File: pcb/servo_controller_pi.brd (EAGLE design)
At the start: 111 parts, among them IC1 PIC18F452, IC2 DS1339, IC3 MAX4173FESA+, IC4 LM2936MP-3.3, IC6 LM386M-1, IC7 GY-27, IC8 MCP23017SO, Q1 10Mhz

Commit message: BleuettePi new modification
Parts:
- removed IC8: MCP23017SO, adafruit:SO28W
- removed SV3: (no value), con-lstb:MA05-2
- added IC5: MCP23017SS, adafruit:SSOP28
- added X1: (no value), con-wago-500:W237-4
- SV1: device con-lstb:MA04-1 -> con-lstb:MA05-2
- SV2: device con-lstb:MA08-2 -> con-lstb:MA05-2
- moved SV1 78.2 mm to (75.6, 51.4), turned to 180 degrees
- moved TP1 20.3 mm to (1.75, 15.6)
- moved S11 10.5 mm to (66.4, 4.45)
- moved S10 10.2 mm to (62.9, 4.45)
- moved SV2 10.2 mm to (61.6, 51.4)
- moved S9 8.57 mm to (59.4, 4.45)
- moved S8 8.26 mm to (55.9, 4.45)
- moved SX 8.09 mm to (22.5, 10.8), turned to 0 degrees
- moved C3 7.85 mm to (11.4, 30.5), flipped to the bottom
- moved S7 6.03 mm to (52.4, 4.45)
- moved S6 5.71 mm to (48.9, 4.45)
- moved T_6V 5.40 mm to (46.4, 7.30)
- moved C9 5.08 mm to (43.2, 4.76)
- moved R1 4.94 mm to (11.4, 22.2), turned to 180 degrees
- moved S5 4.13 mm to (37.5, 4.45)
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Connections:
- removed net OUT: U$3.12
- new net OPTION4: U$3.21
- net +5V: now also IC5.18, IC5.9, SV1.10, SV2.10, X1.2; no longer IC8.18, IC8.9, SV1.2, SV3.10
- net +7V: now also X1.3; no longer SV1.3
- net GPA0: now also IC5.21, SV1.1; no longer IC8.21, SV2.2
- net GPA1: now also IC5.22, SV1.2; no longer IC8.22, SV2.4
- net GPA2: now also IC5.23, SV1.3; no longer IC8.23, SV2.6
- net GPA3: now also IC5.24, SV1.4; no longer IC8.24, SV2.8
- net GPA4: now also IC5.25, SV1.5; no longer IC8.25, SV2.10
- net GPA5: now also IC5.26, SV1.6; no longer IC8.26, SV2.12
- net GPA6: now also IC5.27, SV1.7; no longer IC8.27, SV2.14
- net GPA7: now also IC5.28, SV1.8; no longer IC8.28, SV2.16
- net GPB0: now also IC5.1, SV2.1; no longer IC8.1, SV3.2
- net GPB1: now also IC5.2, SV2.2; no longer IC8.2, SV3.1
- net GPB2: now also IC5.3, SV2.3; no longer IC8.3, SV3.4
- net GPB3: now also IC5.4, SV2.4; no longer IC8.4, SV3.3
- net GPB4: now also IC5.5, SV2.5; no longer IC8.5, SV3.6
- net GPB5: now also IC5.6, SV2.6; no longer IC8.6, SV3.5
- net GPB6: now also IC5.7, SV2.7; no longer IC8.7, SV3.8
- net GPB7: now also DRDY.1, IC5.8, SV2.8; no longer IC8.8, SV3.7
- net INTA: now also IC5.20; no longer IC8.20
- net INTB: now also IC5.19; no longer IC8.19
- net INTD: now also U$3.12; no longer DRDY.1
- net OPTION2: now also U$3.13; no longer U$3.16
- net OPTION3: now also U$3.15; no longer U$3.13
- net SCL: now also IC5.12; no longer IC8.12
- net SDA: now also IC5.13; no longer IC8.13
- net TRIGGER: now also U$3.16; no longer U$3.15
- net VDD: now also X1.4; no longer SV1.4
- net VSS: now also IC5.10, IC5.15, IC5.16, IC5.17, SV1.9, X1.1; no longer IC8.10, IC8.15, IC8.16, IC8.17, SV1.1, SV2.1, SV2.11, SV2.13, SV2.15, SV2.3, SV2.5, SV2.7, SV3.9
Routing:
- net +5V: track 306.3 -> 262.4 mm, vias 7 -> 6
- net VEE: track 172.1 -> 137.4 mm
- net INTB: track 57.0 -> 22.8 mm, vias 2 -> 0
- net INTA: track 51.6 -> 20.6 mm, vias 2 -> 0
- net OUT: track 25.7 -> 0.00 mm
- net +7V: track 40.8 -> 17.0 mm
- net GPB7: track 26.8 -> 10.8 mm
- net GPB6: track 27.4 -> 13.2 mm
- net +3V3: track 103.1 -> 91.2 mm
- net N$19: track 21.7 -> 10.8 mm
- net GPB4: track 21.5 -> 10.8 mm
- net SS11: track 35.6 -> 25.1 mm
- net SS10: track 31.5 -> 21.3 mm
- net VDD: track 8.65 -> 0.00 mm
- net SS9: track 25.7 -> 17.2 mm
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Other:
- board text added: "Isoler la partie ADC et SON"
- board text removed: "Isoler la partie ADC"

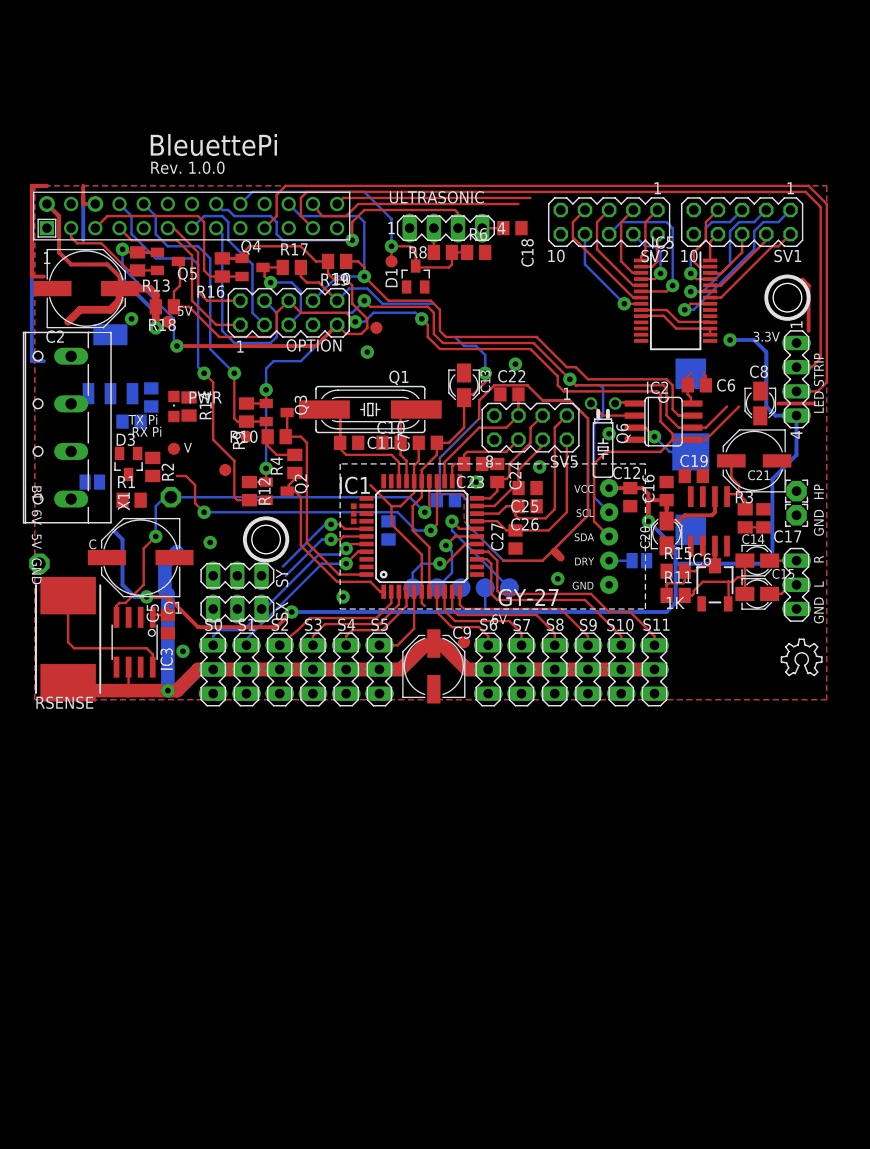
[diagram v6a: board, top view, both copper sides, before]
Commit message: Routage BleuettePi
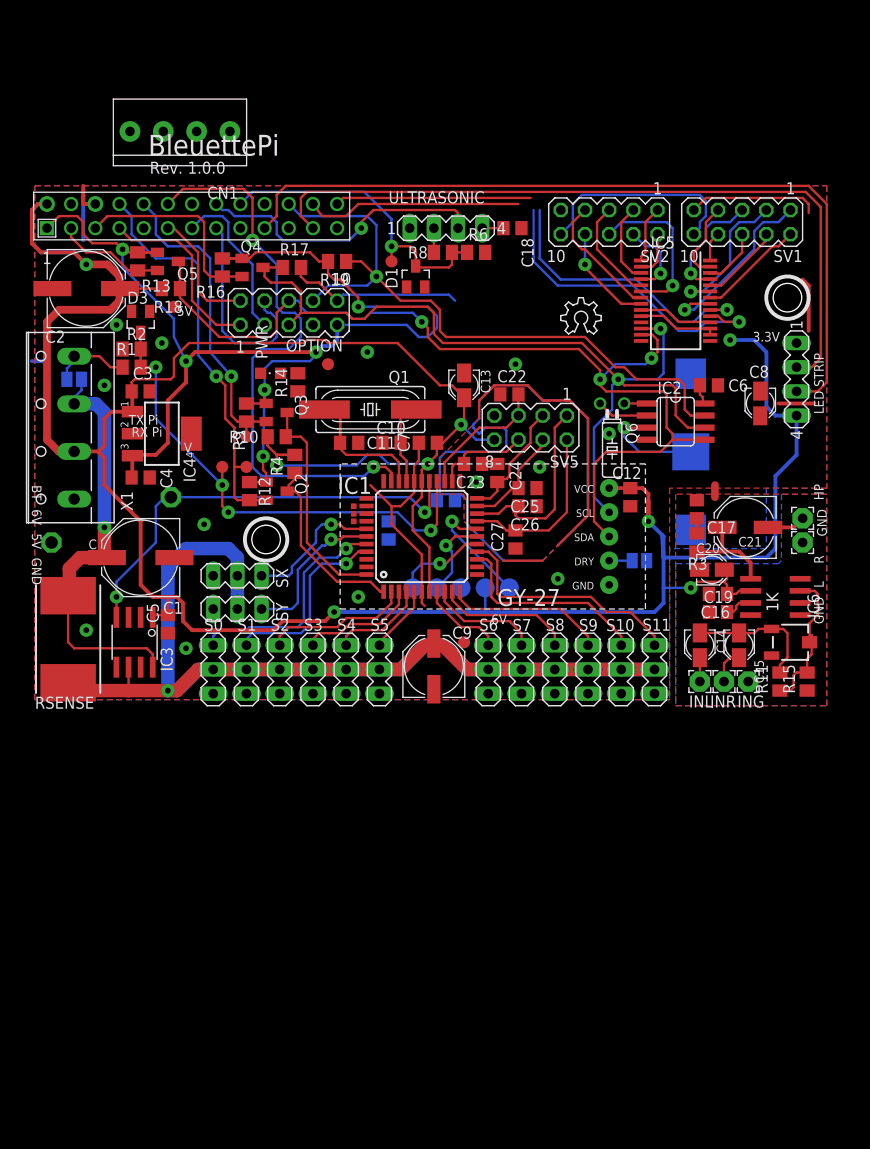
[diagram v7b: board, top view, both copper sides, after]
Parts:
- removed SV4: (no value), con-lstb:MA03-1
- added CN1: 1X4-3.5MM, adafruit:1X04-3.5MM
- added ING, INL, INR: (no value), wirepad:2,15/1,0
- moved U$5 42.7 mm to (56.5, 39.7)
- moved R15 18.0 mm to (82.4, 3.17), turned to 90 degrees
- moved D3 15.0 mm to (12.4, 41.0)
- moved C19 14.5 mm to (73.0, 10.5)
- moved R11 14.2 mm to (79.5, 3.17), turned to 90 degrees
- moved R1 14.0 mm to (11.4, 36.2)
- moved R2 12.6 mm to (11.4, 38.1), turned to 0 degrees
- moved C16 12.1 mm to (73.0, 12.4), turned to 180 degrees
- moved R14 11.7 mm to (28.9, 34.6), turned to 90 degrees
- moved J_SERV 11.0 mm to (5.40, 34.9)
- moved PWR 10.7 mm to (26.0, 35.6), turned to 90 degrees
- moved C14 10.7 mm to (71.1, 6.99), turned to 270 degrees
- moved IC6 10.6 mm to (79.1, 12.1), turned to 90 degrees
- moved 1K 9.97 mm to (80.6, 7.30), turned to 0 degrees
- moved IC4 9.08 mm to (14.6, 29.2), flipped to the top, turned to 270 degrees
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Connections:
- net N$40: now also INR.1; no longer SV4.2
- net N$7: now also 1K.1; no longer 1K.3
- net N$8: now also INL.1; no longer SV4.3
- net VSS: now also 1K.3, ING.1; no longer 1K.1, SV4.1
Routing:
- net +5V: track 262.4 -> 372.4 mm, vias 6 -> 8
- net INTD: track 0.00 -> 61.4 mm, vias 0 -> 2
- net +3V3: track 91.2 -> 133.5 mm, vias 4 -> 6
- net INTB: track 22.8 -> 56.5 mm, vias 0 -> 1
- net INTA: track 20.6 -> 50.4 mm, vias 0 -> 1
- net +7V: track 17.0 -> 44.8 mm, vias 0 -> 1
- net VSS: track 87.0 -> 67.0 mm, vias 8 -> 11
- net AN6: track 35.6 -> 53.0 mm, vias 2 -> 4
- net VEE: track 137.4 -> 149.0 mm
- net VDD: track 0.00 -> 8.29 mm
- net N$41: track 9.74 -> 16.7 mm
- net SCL: track 84.2 -> 90.5 mm, vias 3 -> 2
- net N$24: track 10.2 -> 16.2 mm
- net SDA: track 97.7 -> 102.1 mm, vias 2 -> 3
- net AGND: track 93.6 -> 97.8 mm
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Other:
- board text removed: "Isoler la partie ADC et SON"

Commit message: BleuettePi...
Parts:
- removed C3: 100nf, rcl:C0805
- removed C4: 10uf, rcl:C0805
- removed D1: 3V3, diode:SOT23
- removed IC4: LM2936MP-3.3, national-semiconductor:SOT223
- removed LED-STRIP, ULTRASONIC: (no value), con-lstb:MA04-1
- removed OPTION: (no value), con-lstb:MA05-2
- removed Q2, Q3, Q4, Q5: (no value), adafruit:SOT23
- removed R12, R4: 1k, rcl:M0805
- removed R13, R16, R17, R18: 10k, rcl:M0805
- removed R6: 3k3, rcl:M0805
- removed R8: 2k2, rcl:M0805
- removed T_ECHO, T_TX_PI: TPB1,27, testpad:B1,27
- removed U$7: (no value), adafruit:CR1220-SMD
- added C30, C31: 100nf, rcl:C0805
- added JP1: (no value), jumper:JP1
- added SJ1, SJ2: (no value), jumper:SJ_2
- added SV3: (no value), con-lstb:MA07-1
- added SV4: (no value), con-lstb:MA05-2
- added SV6: (no value), con-lstb:MA04-1
- added SV7: (no value), con-lstb:MA20-1
- added U$1: (no value), adafruit:CR1220-THM
- added U1, U2: (no value), adafruit:TSSOP20
- C18: value (none) -> 100nf
- C8: value (none) -> 100nf; device rcl:PANASONIC_A -> rcl:C0805
- R10: value 2k2 -> CALCUL_ME
- R9: value 3k3 -> CALCUL_ME
- moved C8 37.0 mm to (41.6, 41.3), turned to 180 degrees
- moved D3 21.3 mm to (25.4, 24.1), turned to 90 degrees
- moved R2 18.8 mm to (21.6, 22.2)
- moved R1 15.8 mm to (21.6, 24.1)
- moved T_5V 15.0 mm to (28.6, 34.6)
- moved R19 12.6 mm to (41.6, 38.1), turned to 0 degrees
- moved T_3.3V 12.2 mm to (44.1, 38.1)
- moved C18 11.3 mm to (40.6, 47.6), turned to 90 degrees
- moved C6 7.94 mm to (64.1, 34.0), turned to 0 degrees
- moved PWR 7.47 mm to (18.7, 37.1)
- moved R14 7.13 mm to (22.2, 37.1), turned to 180 degrees
- moved DRDY 5.02 mm to (60.0, 14.3), turned to 180 degrees
- moved Q6 4.48 mm to (63.7, 28.3), turned to 0 degrees
- moved R9 3.18 mm to (25.4, 28.9), turned to 0 degrees
- moved R10 2.29 mm to (25.4, 30.8)
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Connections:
- removed net DI: LED-STRIP.3, U$3.19
- removed net ECHO: D1.3, R6.2, R8.1, T_ECHO.TP, U$3.18
- removed net N$15: R8.2, ULTRASONIC.2
- removed net SI: LED-STRIP.2, U$3.23
- removed net TRIGGER: U$3.16, ULTRASONIC.3
- new net CE0: SV3.4, U2.16
- new net CE1: SV3.5, U2.15
- new net J_PI_CE1: SJ1.3, U2.6
- new net J_PI_INTA: SJ1.1, U2.7
- new net MISO: SV3.2, U2.18
- new net MOSI: SV3.1, U2.20
- new net PI_CE0: U$3.24, U2.5
- new net PI_CE1: SJ1.2, U$3.26
- new net PI_INTB: U$3.15, U2.8
- new net PI_INTD: U$3.12, U2.9
- new net PI_MISO: U$3.21, U2.3
- new net PI_MOSI: U$3.19, U2.1
- new net PI_OPTION0: U$3.7, U1.7
- new net PI_OPTION1: U$3.11, U1.6
- new net PI_OPTION2: U$3.13, U1.3
- new net PI_OPTION3: U$3.16, U1.4
- new net PI_OPTION4: U$3.18, U1.5
- new net PI_SCLK: U$3.23, U2.4
- new net SCLK: SV3.3, U2.17
- net +3V3: now also C30.1, C8.1, U1.10, U1.2, U2.10, U2.2; no longer C4.1, IC4.3, OPTION.9, Q2.1, Q3.1, Q4.1, Q5.1, R12.2, R13.2, R16.2, R9.2
- net +5V: now also C31.1, SV3.7, SV4.10, SV6.1, U1.19, U2.19; no longer C3.1, C8.+, IC4.1, LED-STRIP.4, OPTION.10, R10.2, R17.2, R18.2, R4.2, ULTRASONIC.4
- net +7V: now also JP1.1
- net INTA: now also U2.14; no longer U$3.26
- net INTB: now also U2.13; no longer U$3.24
- net INTC: now also SV4.6; no longer OPTION.8
- net INTD: now also U2.12; no longer U$3.12
- net N$16: now also R9.2; no longer Q3.3, R10.1
- net N$58: now also U$1.-; no longer U$7.-
- net OPTION0: now also SV4.1, U1.14; no longer OPTION.1, U$3.7
- net OPTION1: now also SV4.2, U1.15; no longer OPTION.2, U$3.11
- net OPTION2: now also SV4.3, U1.18; no longer OPTION.3, U$3.13
- net OPTION3: now also SV4.4, SV6.2, U1.17; no longer OPTION.4, U$3.15
- net OPTION4: now also SV4.5, SV6.3, U1.16; no longer U$3.21
- net PI_SCL: now also U1.8; no longer Q4.2, R16.1
- net PI_SDA: now also U1.9; no longer Q5.2, R13.1
- net RX_PI: now also R10.2; no longer Q3.2
- net RX_PIC: now also U1.20; no longer Q2.3, R4.1
- net SCL: now also SV4.7, U1.13; no longer OPTION.5, Q4.3, R17.1
- net SDA: now also SV4.8, U1.12; no longer OPTION.6, Q5.3, R18.1
- net TX_PI: now also U1.1; no longer Q2.2, R12.1, T_TX_PI.TP
- net VDD: now also JP1.2
- net VSS: now also C30.2, C31.2, C8.2, R10.1, SV3.6, SV4.9, SV6.4, U$1.+1, U$1.+2, U1.11, U2.11; no longer C3.2, C4.2, C8.-, D1.1, IC4.2, IC4.4, LED-STRIP.1, OPTION.7, R6.1, U$7.+$1, U$7.+$2, ULTRASONIC.1
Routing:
- net DI: track 85.3 -> 0.00 mm
- net SI: track 78.0 -> 0.00 mm
- net PI_INTD: track 0.00 -> 40.3 mm, vias 0 -> 1
- net ECHO: track 33.1 -> 0.00 mm, vias 1 -> 0
- net PI_INTB: track 0.00 -> 32.8 mm, vias 0 -> 2
- net TX_PI: track 42.7 -> 11.1 mm, vias 1 -> 0
- net TRIGGER: track 31.1 -> 0.00 mm, vias 1 -> 0
- net GPB7: track 11.0 -> 41.7 mm, vias 1 -> 2
- net RX_PIC: track 19.7 -> 48.0 mm, vias 0 -> 2
- net +3V3: track 133.5 -> 106.4 mm, vias 6 -> 4
- net PI_CE0: track 0.00 -> 22.5 mm
- net VDD: track 8.29 -> 29.4 mm, vias 0 -> 1
- net SDA: track 102.1 -> 81.2 mm
- net PI_MOSI: track 0.00 -> 20.7 mm
- net PI_CE1: track 0.00 -> 19.9 mm
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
